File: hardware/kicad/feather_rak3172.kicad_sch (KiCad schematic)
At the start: 51 parts, among them J1 Pin Header, J2 Pin Header, J3 USB_C_Receptacle_USB2.0, J4 915MHz SMA, J5 SWD, J6 JST-2PH, Q1 DMG341, SW1 RESET, SW2 BOOT, U1 RAK3172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

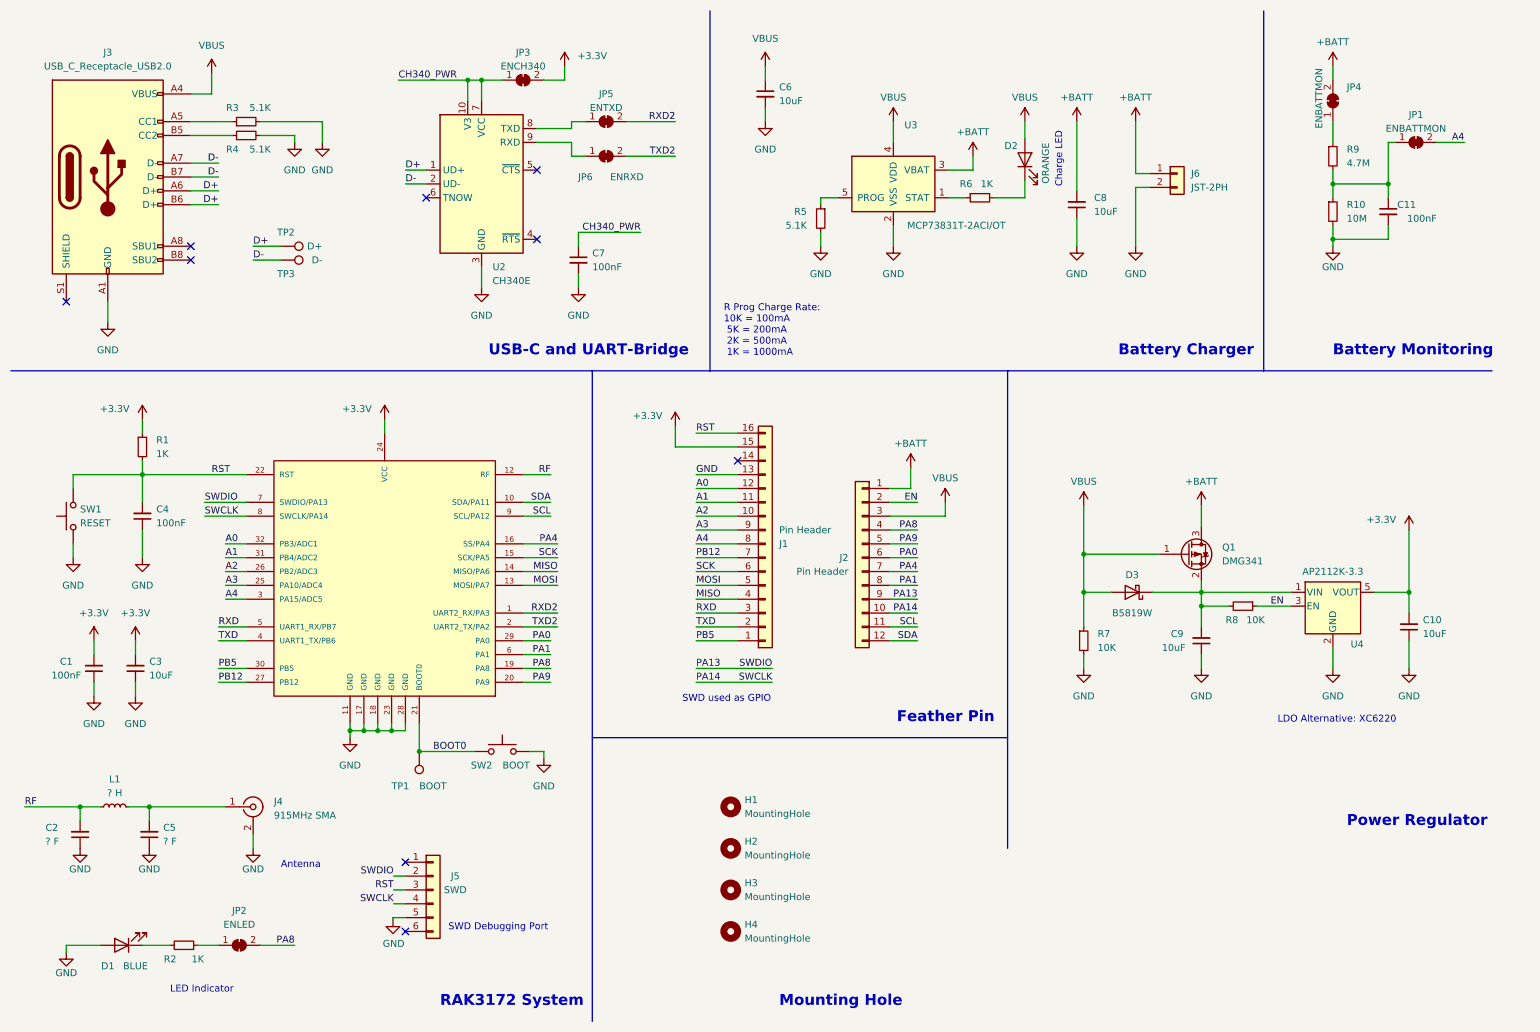
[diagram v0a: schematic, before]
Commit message: change solder jump to open, and minor component description changes
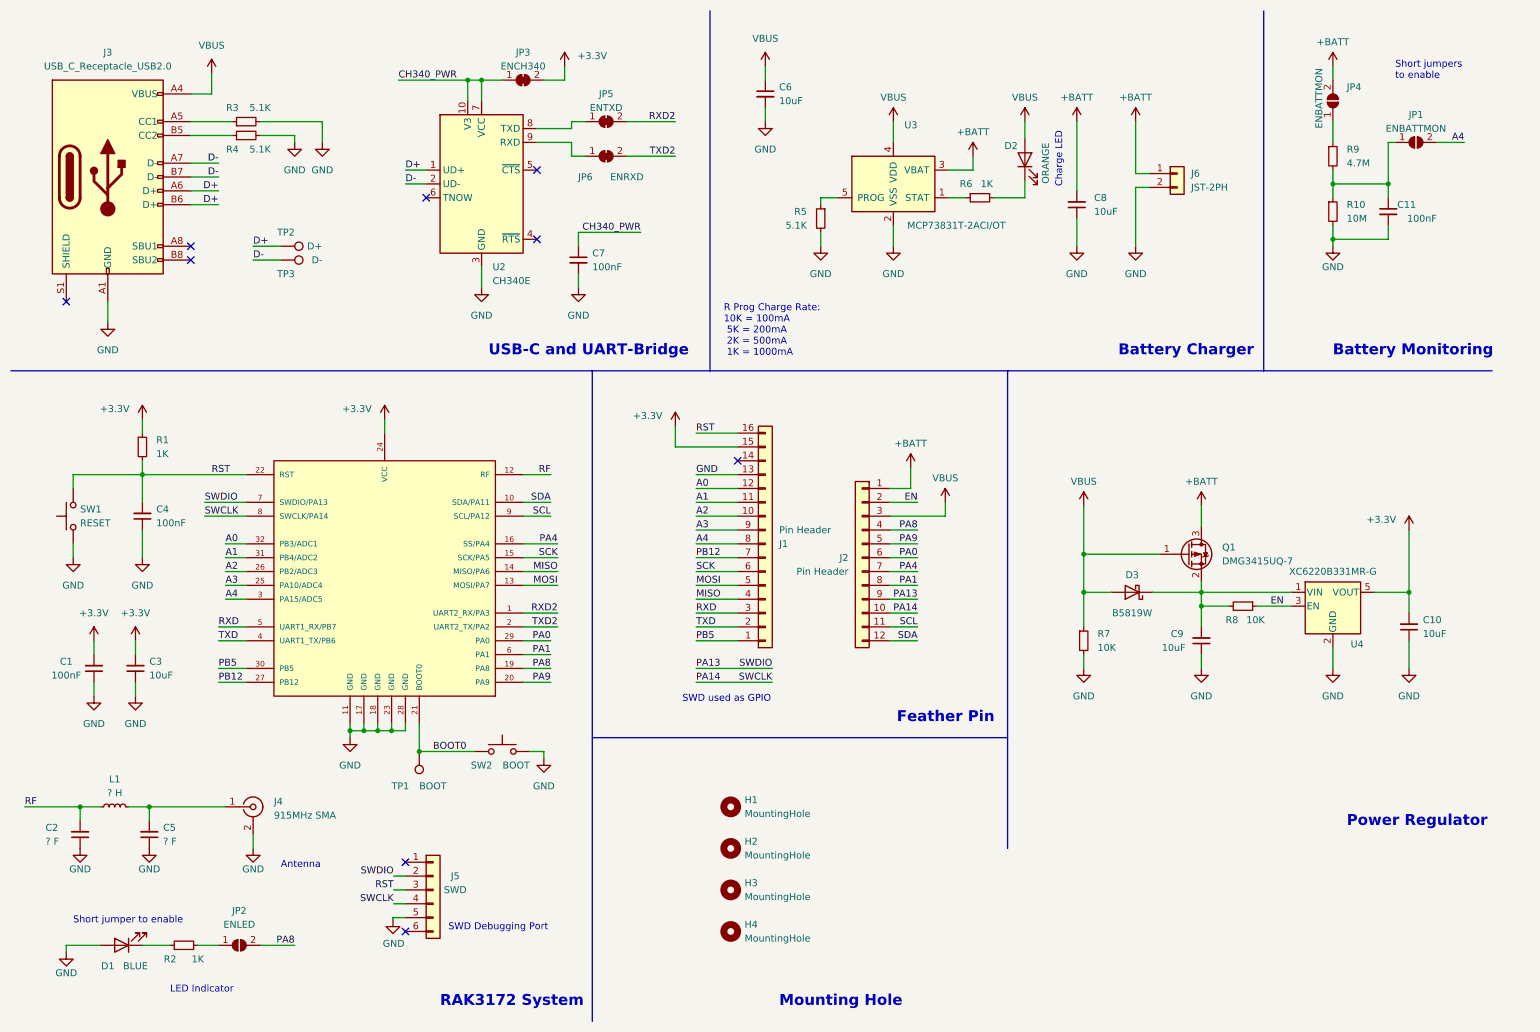
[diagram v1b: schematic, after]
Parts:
- D1: Part Description Red 2V 20mA -> Blue 2V 25mA
- D2: Part Number Orange 2V 20mA -> Orange 2V 25mA
- JP1, JP2, JP4: footprint Jumper:SolderJumper-2_P1.3mm_Bridged_RoundedPad1.0x1.5mm -> Jumper:SolderJumper-2_P1.3mm_Open_RoundedPad1.0x1.5mm; symbol Jumper:SolderJumper_2_Bridged -> Jumper:SolderJumper_2_Open
- Q1: value DMG341 -> DMG3415UQ-7
- U4: value AP2112K-3.3 -> XC6220B331MR-G; Manufacturer Diodes Incorporated -> Torex Semiconductor; Part Number AP2112K-3.3TRG1 -> XC6220B331MR-G
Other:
- note added: "Short jumper to enable"
- note added: "Short jumpers to enable"
- note removed: "LDO Alternative: XC6220"
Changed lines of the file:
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@@
+    (effects (font (size 1.27 1.27)) (justify left bottom))
+  )
+  (text "Short jumpers \nto enable" (at 266.7 25.4 0)
+    (effects (font (size 1.27 1.27)) (justify left bottom))
+  )
+  (text "Short jumper to enable" (at 24.13 180.34 0)
     (effects (font (size 1.27 1.27)) (justify left bottom))
   )
@@
   (text "Battery Charger" (at 215.9 76.2 0)
     (effects (font (size 2 2) (thickness 0.4) bold) (justify left bottom))
-  )
-  (text "LDO Alternative: XC6220" (at 245.11 143.51 0)
-    (effects (font (size 1.27 1.27)) (justify left bottom))
   )
   (text "Feather Pin" (at 175.26 143.51 0)
@@
       (effects (font (size 1.27 1.27)) hide)
     )
-    (property "Part Number" "Orange 2V 20mA" (id 4) (at 198.755 40.005 90)
+    (property "Part Number" "Orange 2V 25mA" (id 4) (at 198.755 40.005 90)
       (effects (font (size 1.27 1.27)) hide)
     )
@@
       (effects (font (size 1.27 1.27)) hide)
     )
-    (property "Part Description" "Red 2V 20mA" (id 4) (at 33.02 184.15 0)
+    (property "Part Description" "Blue 2V 25mA" (id 4) (at 33.02 184.15 0)
       (effects (font (size 1.27 1.27)) hide)
     )
@@
     (pin "1")
   )
-  (symbol (lib_id "Jumper:SolderJumper_2_Bridged") (at 54.61 184.15 0) (unit 1)
+  (symbol (lib_id "Jumper:SolderJumper_2_Open") (at 54.61 184.15 0) (unit 1)
     (in_bom yes) (on_board yes) (fields_autoplaced)
     (property "Reference" "JP2" (id 0) (at 54.61 177.8 0))
     (property "Value" "ENLED" (id 1) (at 54.61 180.34 0))
-    (property "Footprint" "Jumper:SolderJumper-2_P1.3mm_Bridged_RoundedPad1.0x1.5mm" (id 2) (at 54.61 184.15 0)
+    (property "Footprint" "Jumper:SolderJumper-2_P1.3mm_Open_RoundedPad1.0x1.5mm" (id 2) (at 54.61 184.15 0)
       (effects (font (size 1.27 1.27)) hide)
     )
@@
     (pin "1")
   )
-  (symbol (lib_id "Jumper:SolderJumper_2_Bridged") (at 270.51 36.83 0) (unit 1)
+  (symbol (lib_id "Jumper:SolderJumper_2_Open") (at 270.51 36.83 0) (unit 1)
     (in_bom yes) (on_board yes)
     (property "Reference" "JP1" (id 0) (at 270.51 31.75 0))
     (property "Value" "ENBATTMON" (id 1) (at 270.51 34.29 0))
-    (property "Footprint" "Jumper:SolderJumper-2_P1.3mm_Bridged_RoundedPad1.0x1.5mm" (id 2) (at 270.51 36.83 0)
+    (property "Footprint" "Jumper:SolderJumper-2_P1.3mm_Open_RoundedPad1.0x1.5mm" (id 2) (at 270.51 36.83 0)
       (effects (font (size 1.27 1.27)) hide)
     )
@@
       (effects (font (size 1.27 1.27)) (justify left))
     )
-    (property "Value" "DMG341" (id 1) (at 234.95 113.6649 0)
+    (property "Value" "DMG3415UQ-7" (id 1) (at 234.95 113.6649 0)
       (effects (font (size 1.27 1.27)) (justify left))
     )
@@
     (in_bom yes) (on_board yes)
     (property "Reference" "U4" (id 0) (at 259.715 128.905 0))
-    (property "Value" "AP2112K-3.3" (id 1) (at 255.27 115.57 0))
+    (property "Value" "XC6220B331MR-G" (id 1) (at 255.27 115.57 0))
     (property "Footprint" "Package_TO_SOT_SMD:SOT-23-5" (id 2) (at 255.27 113.665 0)
       (effects (font (size 1.27 1.27)) hide)
     )
-    (property "Datasheet" "https://www.diodes.com/assets/Datasheets/AP2112.pdf" (id 3) (at 255.27 119.38 0)
-      (effects (font (size 1.27 1.27)) hide)
-    )
-    (property "Manufacturer" "Diodes Incorporated" (id 4) (at 255.27 121.92 0)
-      (effects (font (size 1.27 1.27)) hide)
-    )
-    (property "Part Number" "AP2112K-3.3TRG1" (id 5) (at 255.27 121.92 0)
+    (property "Datasheet" "https://www.mouser.com/datasheet/2/760/TOSL_S_A0010556302_1-2575005.pdf" (id 3) (at 255.27 119.38 0)
+      (effects (font (size 1.27 1.27)) hide)
+    )
+    (property "Manufacturer" "Torex Semiconductor" (id 4) (at 255.27 121.92 0)
+      (effects (font (size 1.27 1.27)) hide)
+    )
+    (property "Part Number" "XC6220B331MR-G" (id 5) (at 255.27 121.92 0)
       (effects (font (size 1.27 1.27)) hide)
     )
@@
     (pin "1")
   )
-  (symbol (lib_id "Jumper:SolderJumper_2_Bridged") (at 255.27 29.21 270) (mirror x) (unit 1)
+  (symbol (lib_id "Jumper:SolderJumper_2_Open") (at 255.27 29.21 270) (mirror x) (unit 1)
     (in_bom yes) (on_board yes)
     (property "Reference" "JP4" (id 0) (at 257.81 26.67 90)
@@
       (effects (font (size 1.27 1.27)) (justify left))
     )
-    (property "Footprint" "Jumper:SolderJumper-2_P1.3mm_Bridged_RoundedPad1.0x1.5mm" (id 2) (at 255.27 29.21 0)
+    (property "Footprint" "Jumper:SolderJumper-2_P1.3mm_Open_RoundedPad1.0x1.5mm" (id 2) (at 255.27 29.21 0)
       (effects (font (size 1.27 1.27)) hide)
     )
@@
     )
     (path "/6b1dbf3b-8902-4f43-9206-9ad674a64600"
-      (reference "JP1") (unit 1) (value "ENBATTMON") (footprint "Jumper:SolderJumper-2_P1.3mm_Bridged_RoundedPad1.0x1.5mm")
+      (reference "JP1") (unit 1) (value "ENBATTMON") (footprint "Jumper:SolderJumper-2_P1.3mm_Open_RoundedPad1.0x1.5mm")
     )
     (path "/62270125-4ebd-4563-8d4e-d2f4b2fb7a04"
-      (reference "JP2") (unit 1) (value "ENLED") (footprint "Jumper:SolderJumper-2_P1.3mm_Bridged_RoundedPad1.0x1.5mm")
+      (reference "JP2") (unit 1) (value "ENLED") (footprint "Jumper:SolderJumper-2_P1.3mm_Open_RoundedPad1.0x1.5mm")
     )
     (path "/b5eab32a-9700-4bc8-9e13-2fa52523106e"
@@
     )
     (path "/f2600352-0328-4d0b-b120-aa592dac6722"
-      (reference "JP4") (unit 1) (value "ENBATTMON") (footprint "Jumper:SolderJumper-2_P1.3mm_Bridged_RoundedPad1.0x1.5mm")
+      (reference "JP4") (unit 1) (value "ENBATTMON") (footprint "Jumper:SolderJumper-2_P1.3mm_Open_RoundedPad1.0x1.5mm")
     )
     (path "/f853e4a3-ea4a-487b-885f-c7b9652dae7b"
@@
     )
     (path "/9a62f1db-3067-412f-b29a-937b11e855ce"
-      (reference "Q1") (unit 1) (value "DMG341") (footprint "Package_TO_SOT_SMD:SOT-23")
+      (reference "Q1") (unit 1) (value "DMG3415UQ-7") (footprint "Package_TO_SOT_SMD:SOT-23")
     )
     (path "/86454675-1629-49ba-a0a7-ae0dbbb2aae3"
@@
     )
     (path "/c9c3b4aa-fb3d-41c3-b4d0-06eb2148dbad"
-      (reference "U4") (unit 1) (value "AP2112K-3.3") (footprint "Package_TO_SOT_SMD:SOT-23-5")
-    )
-  )
+      (reference "U4") (unit 1) (value "XC6220B331MR-G") (footprint "Package_TO_SOT_SMD:SOT-23-5")
+    )
+  )

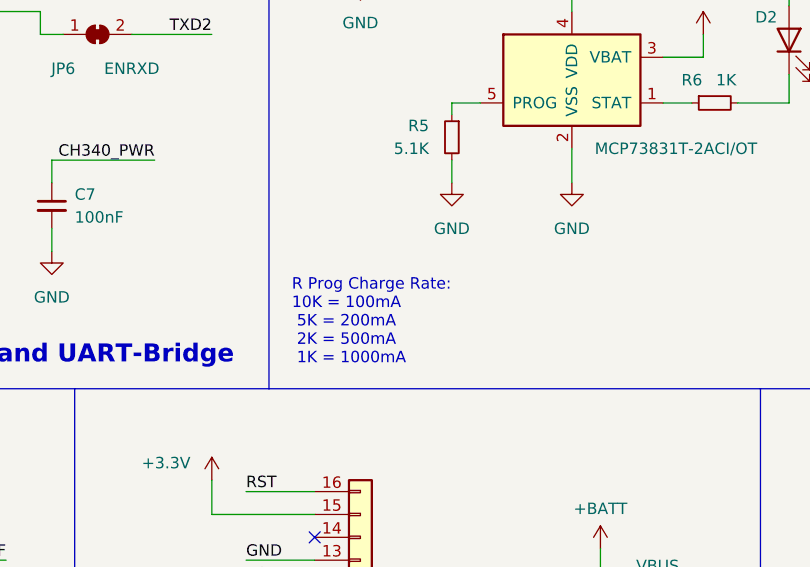
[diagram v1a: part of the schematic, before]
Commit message: update silkscreen version, and minor sch and silkscreen changes
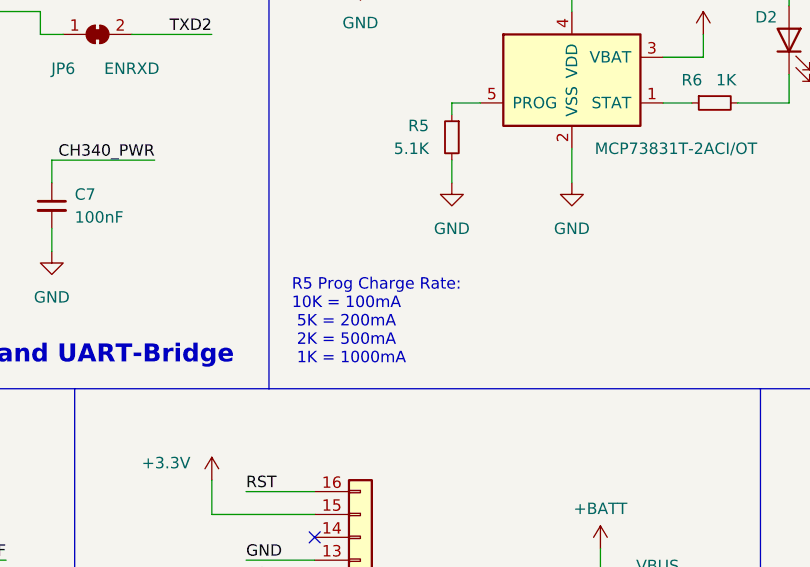
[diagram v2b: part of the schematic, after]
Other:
- note added: "R5 Prog Charge Rate: 10K = 100mA 5K = 200mA 2K = 500mA 1K = 1000mA"
- note removed: "R Prog Charge Rate: 10K = 100mA 5K = 200mA 2K = 500mA 1K = 1000mA"
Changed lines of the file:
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@@
   (title_block
     (title "Feather RAK3172")
-    (date "2023-02-21")
-    (rev "8.1")
+    (date "2023-03-20")
+    (rev "8.2")
     (company "Teapot Laboratories")
   )
@@
     (effects (font (size 2 2) (thickness 0.4) bold) (justify left bottom))
   )
-  (text "R Prog Charge Rate:\n10K = 100mA\n 5K = 200mA\n 2K = 500mA\n 1K = 1000mA"
+  (text "R5 Prog Charge Rate:\n10K = 100mA\n 5K = 200mA\n 2K = 500mA\n 1K = 1000mA"
     (at 143.51 76.2 0)
     (effects (font (size 1.27 1.27)) (justify left bottom))
